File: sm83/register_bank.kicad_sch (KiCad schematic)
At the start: 0 parts

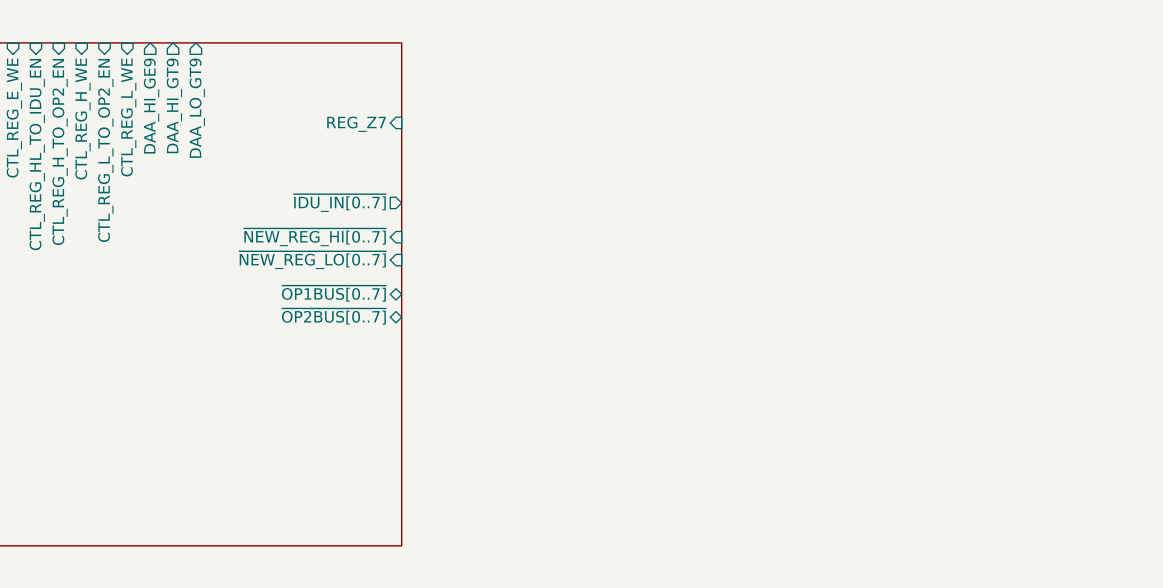
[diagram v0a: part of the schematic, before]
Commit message: SM83: Add schematic for WZ register
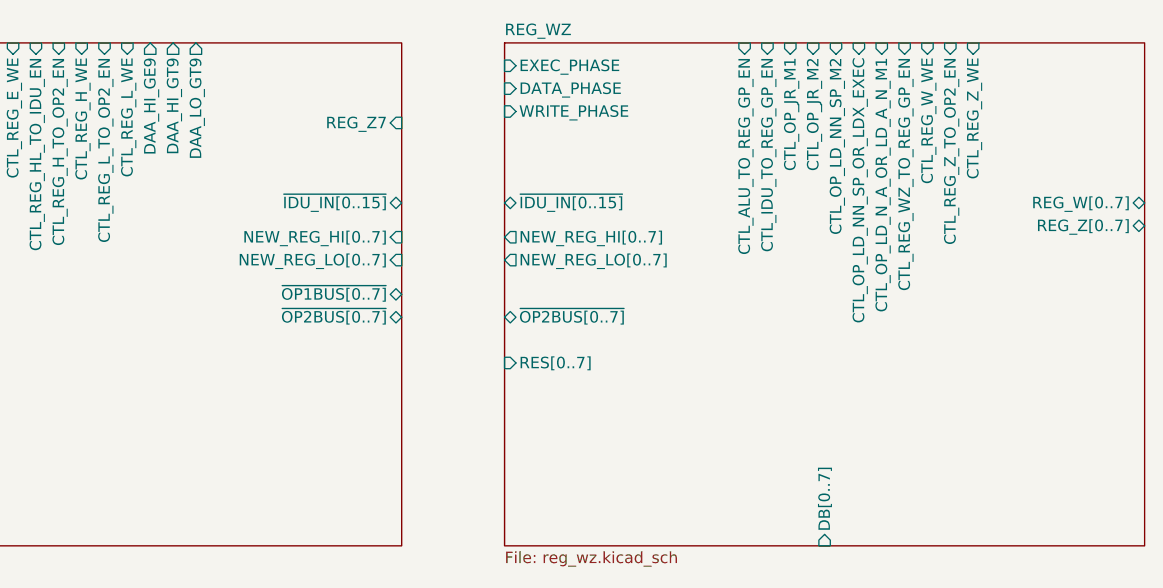
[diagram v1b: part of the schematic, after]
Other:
- added sheet REG_WZ (reg_wz.kicad_sch)
- sheet REG_GP ports: added NEW_REG_HI[0..7], NEW_REG_LO[0..7], ~{IDU_IN[0..15]}; removed ~{IDU_IN[0..7]}, ~{NEW_REG_HI[0..7]}, ~{NEW_REG_LO[0..7]}

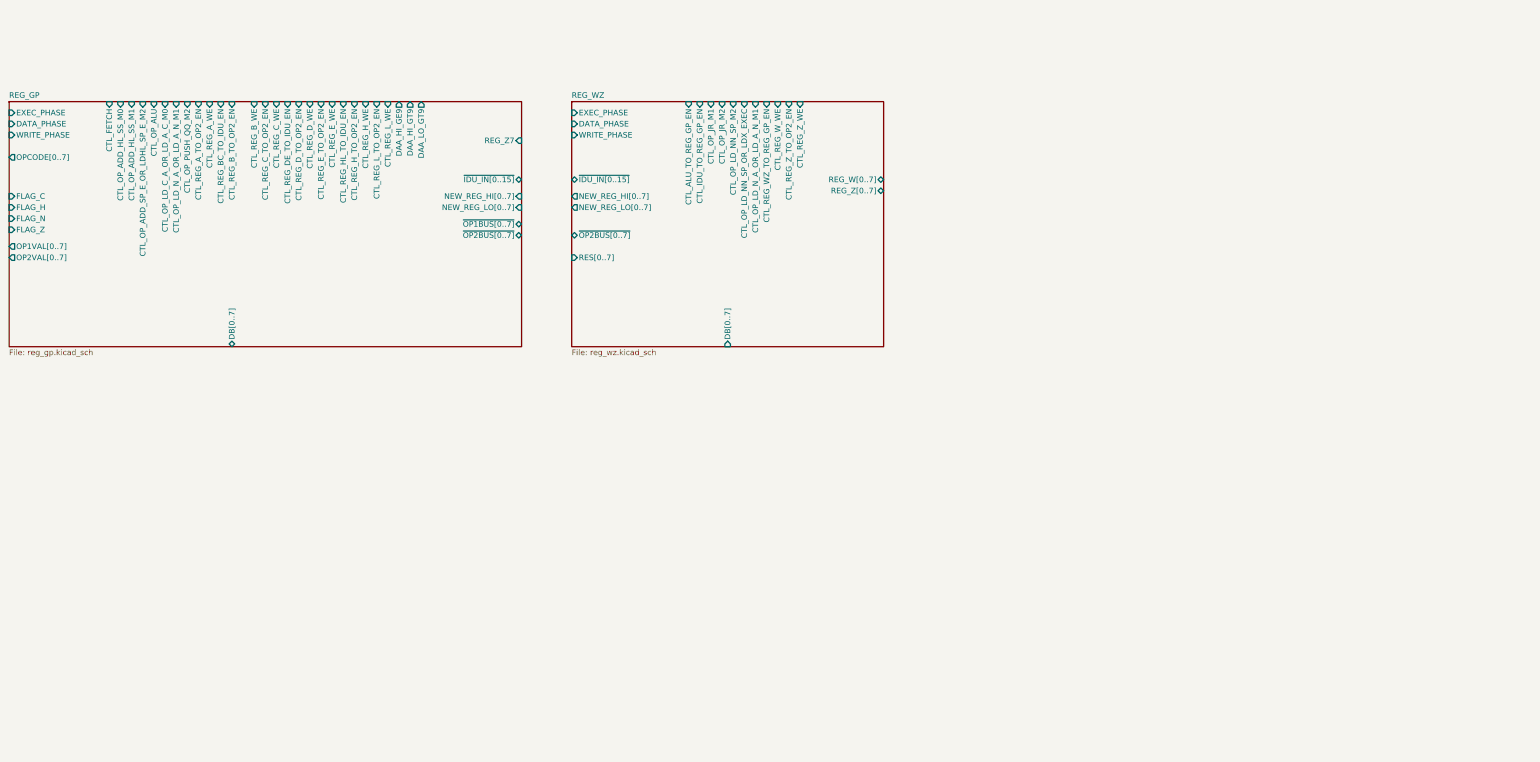
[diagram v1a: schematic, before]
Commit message: SM83: Finish schematics of register bank
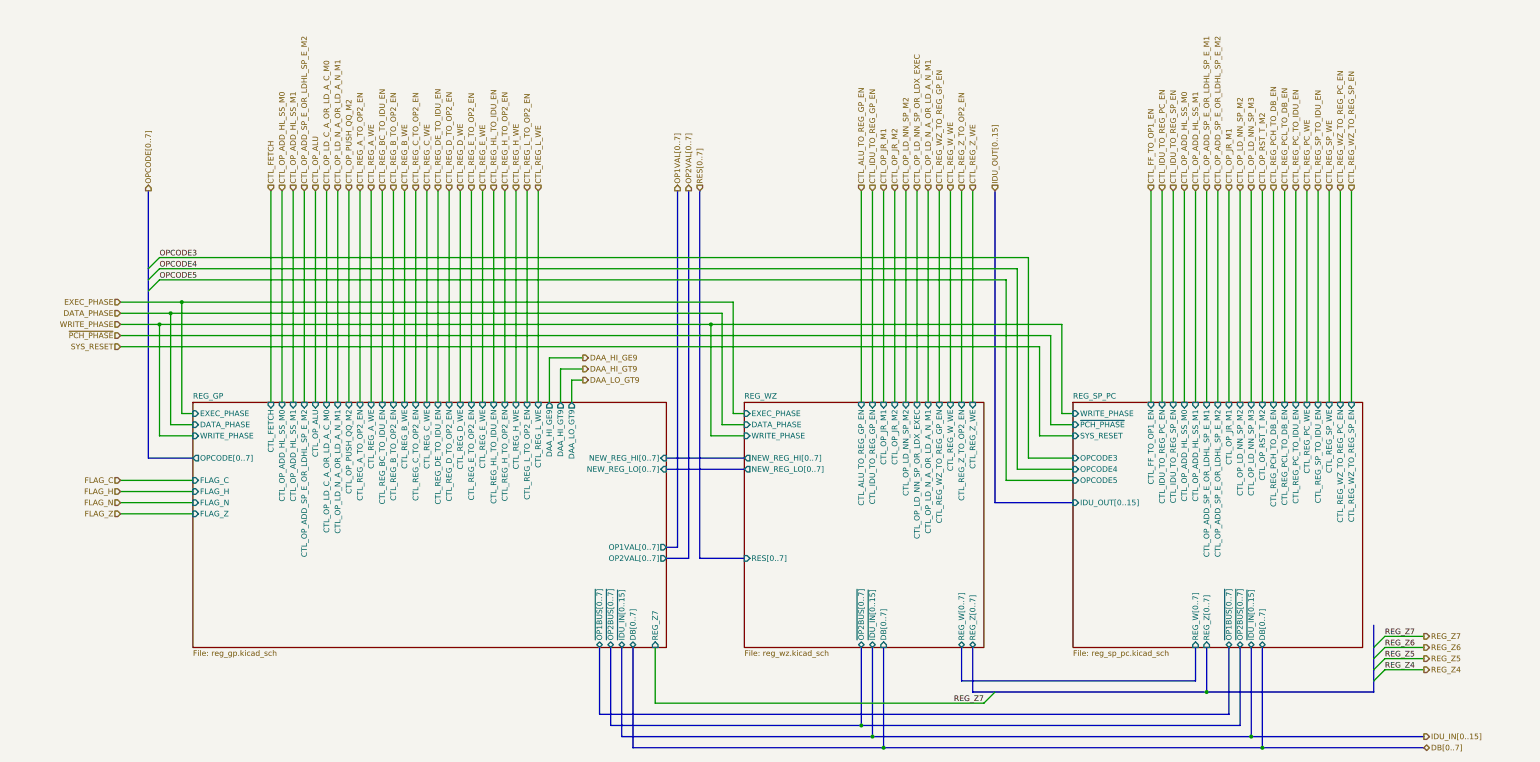
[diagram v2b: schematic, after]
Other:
- added sheet REG_SP_PC (reg_sp_pc.kicad_sch)

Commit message: SM83: Add schematic for interrupt handling
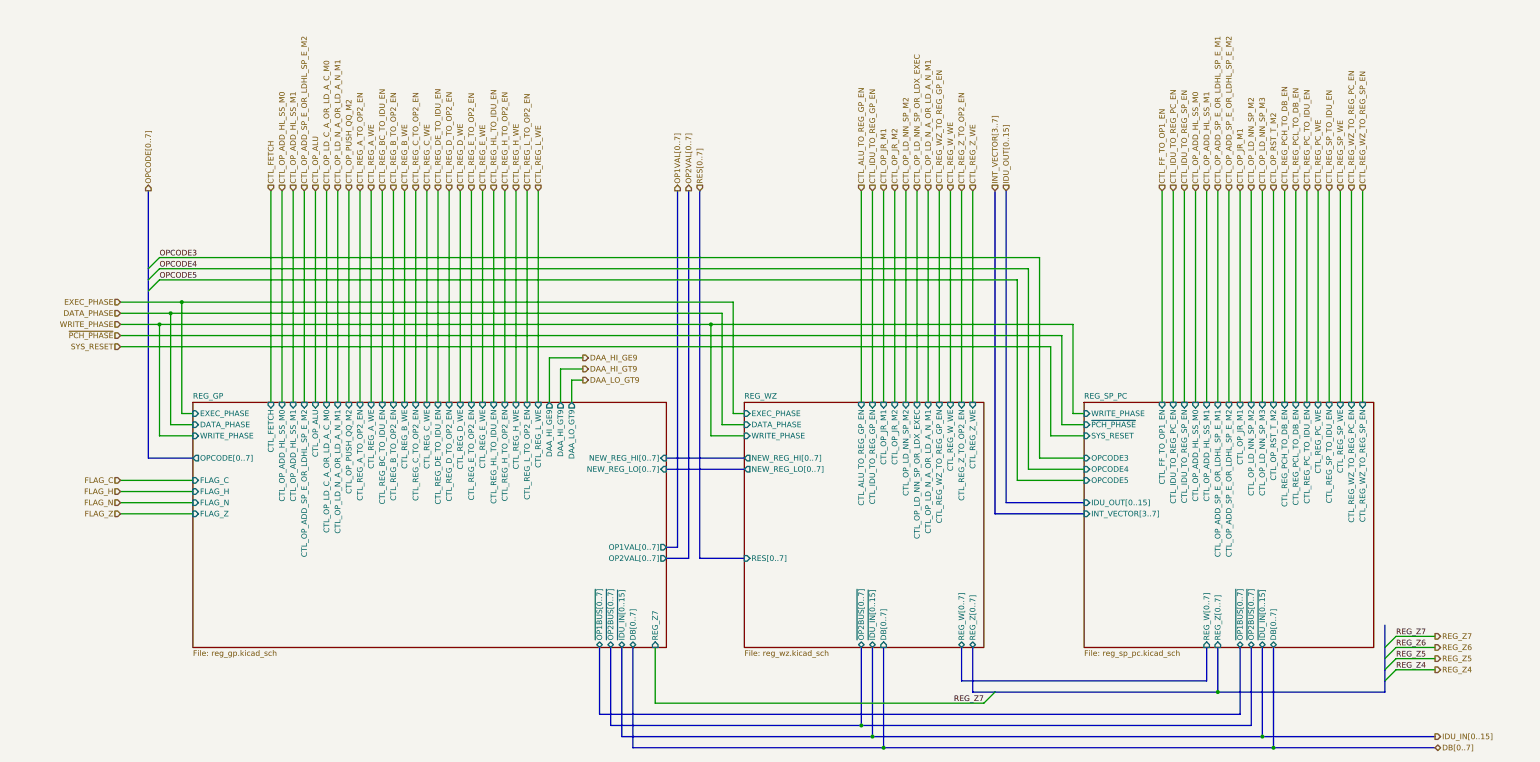
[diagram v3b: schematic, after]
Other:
- sheet REG_SP_PC ports: added INT_VECTOR[3..7]; removed none

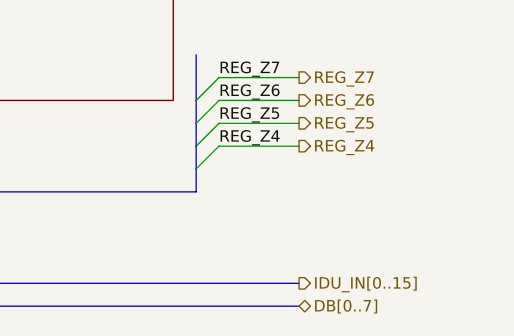
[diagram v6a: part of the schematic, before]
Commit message: SM83: Small IDU fixes
* IDU_INC and IDU_DEC signals were swapped at muxer inputs.
* ~{IDU_IN[0..15]} was missing ~{} in some places.
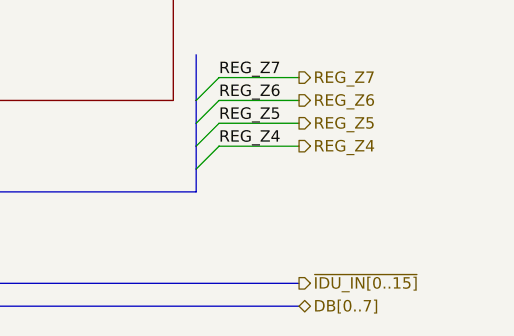
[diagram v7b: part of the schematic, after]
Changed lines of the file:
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@@
 		)
 	)
-	(hierarchical_label "IDU_IN[0..15]"
+	(hierarchical_label "~{IDU_IN[0..15]}"
 		(shape output)
 		(at 358.14 215.9 0)
